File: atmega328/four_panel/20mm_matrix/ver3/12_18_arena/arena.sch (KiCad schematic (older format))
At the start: 50 parts, among them P1 CONN15, P2 CONN15, P3 CONN15, P4 CONN15, P5 CONN15, P6 CONN15, P8 CONN_34X2, P9 CONN_2, Q1 MOSFET_NCHAN, SW1 SWITCH_INV, U1 SPARKFUN_TXB0104, U2 SPARKFUN_TXB0104, U3 SPARKFUN_TXB0104, U4 SPARKFUN_TXB0104, U5 SPARKFUN_TXB0104, U6 SPARKFUN_TXB0104, U8 POLOLU_3V3

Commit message: Finished 12_18 arena schematic.
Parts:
- added C10, C11, C12, C2, C3, C4, C5, C6, C7, C8, C9: C, ~, symbol C
- added C18: 10uf, ~, symbol CP
- added P13, P14, P15, P16, P17, P18, P19, P20, P21, P22, P23, P24: CONN_2, symbol CONN_2
- added R10, R11, R12, R2, R3, R4, R5, R6, R7, R8, R9: R, ~, symbol R
- gave numbers to parts that had none: 20
- renumbered C1 to C13, C2 to C14, C3 to C15, C4 to C16, C5 to C17, P8 to P25, P9 to P26, R3 to R13, R4 to R14, R5 to R15, R6 to R16, R7 to R17, R8 to R18, R1 to R25, R2 to R26, U8 to U13
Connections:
- net 5V: now also C18.1
- net GND: now also C10.2, C11.2, C12.2, C18.2, C2.2, C3.2, C4.2, C5.2, C6.2, C7.2, C8.2, C9.2
- net MISO_10_5V: now also R11.1
- net MISO_11_5V: now also R12.1
- net MISO_1_5V: now also R2.1
- net MISO_2_5V: now also R3.1
- net MISO_3_5V: now also R4.1
- net MISO_4_5V: now also R5.1
- net MISO_5_5V: now also R6.1
- net MISO_6_5V: now also R7.1
- net MISO_7_5V: now also R8.1
- net MISO_8_5V: now also R9.1
- net MISO_9_5V: now also R10.1
- net at C1.1, R1.2: now also P13.2 (PM); no longer U1.11 (B3)
- net at U2.11 (B3): now also P14.1 (P1)
- net at U3.11 (B3): now also P15.1 (P1)
- net at U4.11 (B3): now also P16.1 (P1)
- net at U5.11 (B3): now also P17.1 (P1)
- net at U6.11 (B3): now also P18.1 (P1)
- net at U7.11 (B3): now also P19.1 (P1)
- net at U8.11 (B3): now also P20.1 (P1)
- net at U9.11 (B3): now also P21.1 (P1)
- net at U10.11 (B3): now also P22.1 (P1)
- net at U11.11 (B3): now also P23.1 (P1)
- net at U12.11 (B3): now also P24.1 (P1)
- new net: P13.1 (P1), U1.11 (B3)
- new net: C2.1, P14.2 (PM), R2.2
- new net: C3.1, P15.2 (PM), R3.2
- new net: C4.1, P16.2 (PM), R4.2
- new net: C5.1, P17.2 (PM), R5.2
- new net: C6.1, P18.2 (PM), R6.2
- new net: C7.1, P19.2 (PM), R7.2
- new net: C8.1, P20.2 (PM), R8.2
- new net: C9.1, P21.2 (PM), R9.2
- new net: C10.1, P22.2 (PM), R10.2
- new net: C11.1, P23.2 (PM), R11.2
- new net: C12.1, P24.2 (PM), R12.2
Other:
- moved on the sheet: C1, C13, C14, C15, C16, C17, P1, P10, P11, P12, P2, P25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

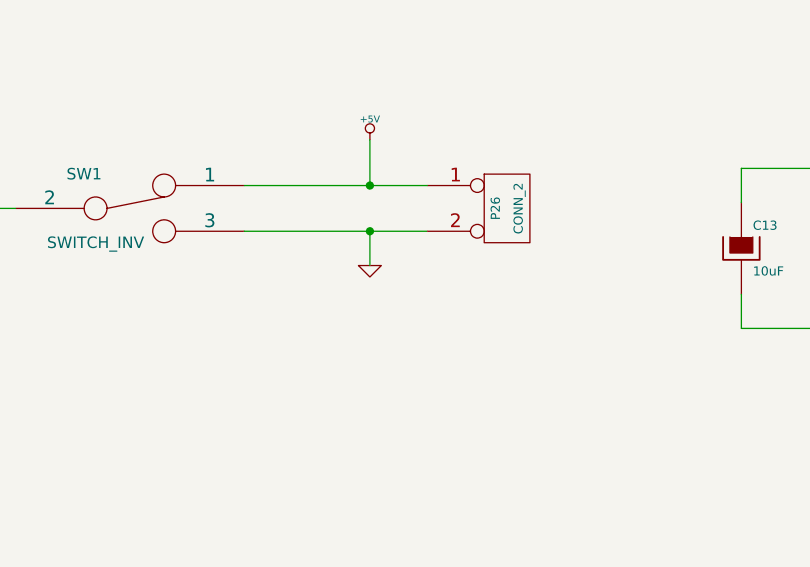
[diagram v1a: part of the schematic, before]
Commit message: Arena modifications.
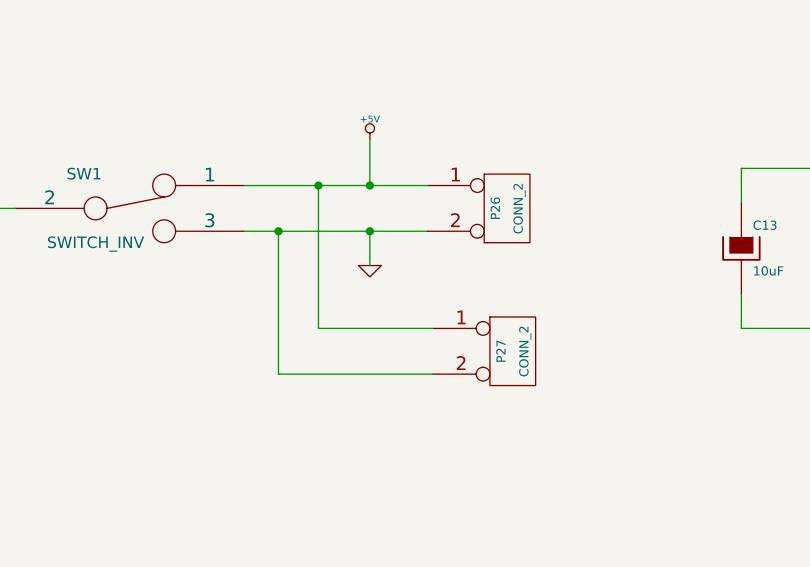
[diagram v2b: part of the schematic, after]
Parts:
- added P27: CONN_2, symbol CONN_2
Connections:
- net +5V: now also P27.1 (P1)
- net GND: now also P27.2 (PM)
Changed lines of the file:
@@
 Sheet 1 1
 Title ""
-Date "8 sep 2015"
+Date "10 sep 2015"
 Rev ""
 Comp ""
@@
 	8550 12250 8550 12500
 Connection ~ 8550 12250
+$Comp
+L CONN_2 P27
+U 1 1 55F1935D
+P 6500 12350
+F 0 "P27" V 6450 12350 40  0000 C CNN
+F 1 "CONN_2" V 6550 12350 40  0000 C CNN
+F 2 "" H 6500 12350 60  0000 C CNN
+F 3 "" H 6500 12350 60  0000 C CNN
+	1    6500 12350
+	1    0    0    -1
+$EndComp
+Wire Wire Line
+	6150 12450 5475 12450
+Wire Wire Line
+	5475 12450 5475 11825
+Connection ~ 5475 11825
+Wire Wire Line
+	6150 12250 5650 12250
+Wire Wire Line
+	5650 12250 5650 11625
+Connection ~ 5650 11625
 $EndSCHEMATC

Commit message: Finished pre-routing layout.
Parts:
- added C19, C20, C21, C22, C23: 10uF, symbol CP
- added P28, P29, P30, P31: CONN_1, symbol CONN_1
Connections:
- net 5V: now also C19.1, C20.1, C21.1, C22.1, C23.1
- net GND: now also C19.2, C20.2, C21.2, C22.2, C23.2, P28.1, P29.1, P30.1, P31.1
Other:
- note added: "Mount holes"
- note removed: "Power"
- moved on the sheet: C13, C14, C15, C16, C17, C18, P26, P27, SW1

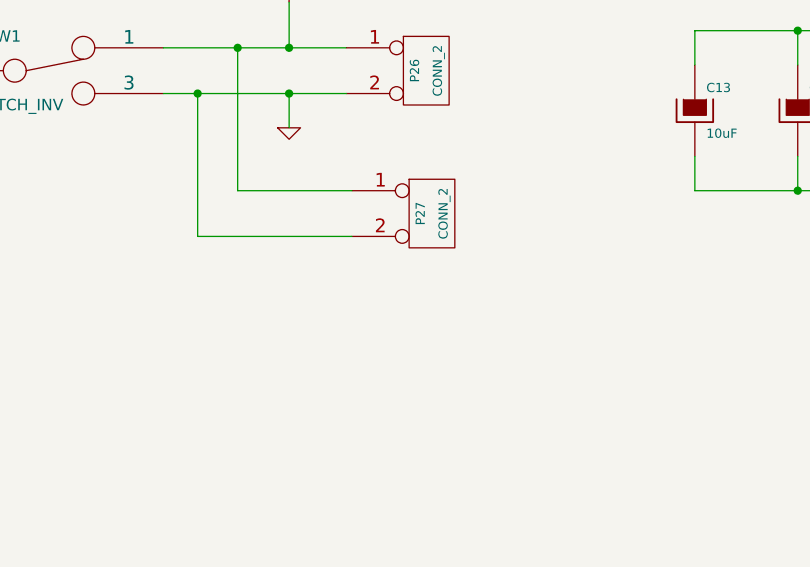
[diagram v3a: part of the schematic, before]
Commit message: Finished design of 12-18 arena. Routed and created gerber files.`
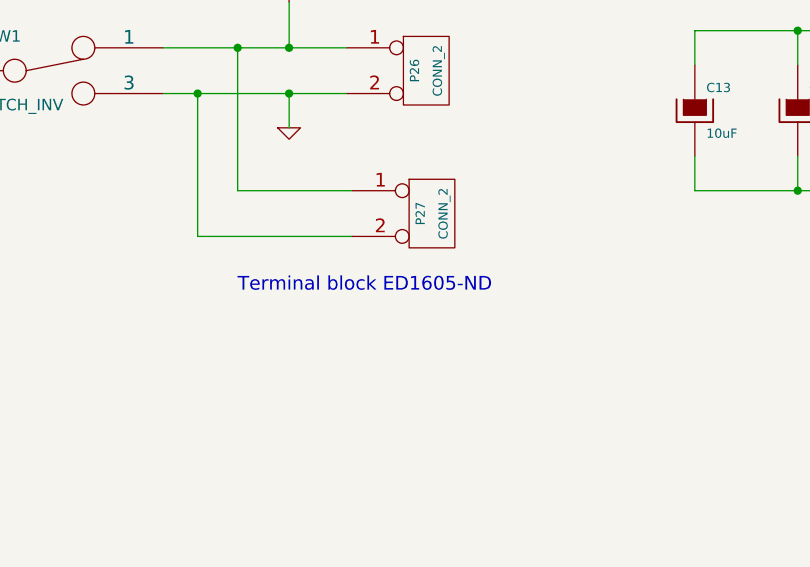
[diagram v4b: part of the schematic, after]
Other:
- note added: "Terminal block ED1605-ND"
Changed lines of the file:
@@
 Text Notes 1600 13800 0    60   ~ 0
 Mount holes
+Text Notes 4350 12650 0    60   ~ 0
+Terminal block ED1605-ND
 $EndSCHEMATC

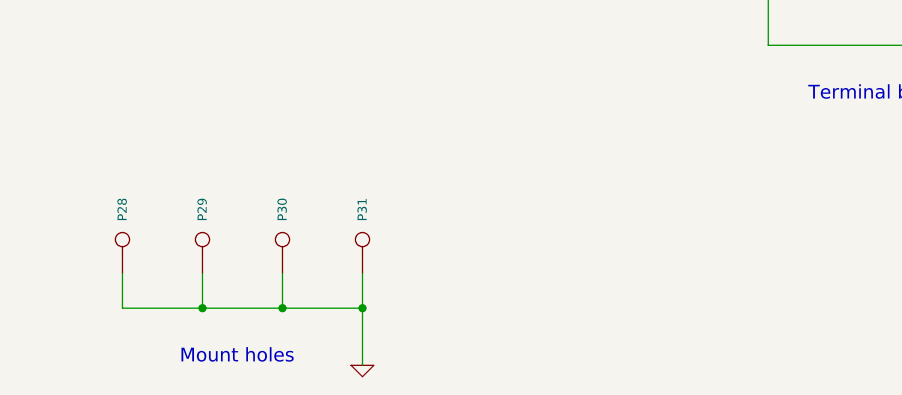
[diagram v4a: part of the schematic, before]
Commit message: Added #4 ground holes.
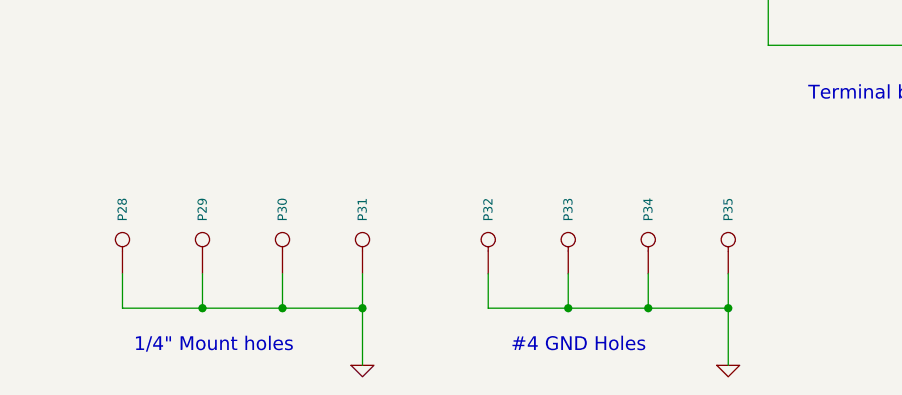
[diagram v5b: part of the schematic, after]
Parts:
- added P32, P33, P34, P35: CONN_1, symbol CONN_1
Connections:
- net GND: now also P32.1, P33.1, P34.1, P35.1
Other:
- note added: "#4 GND Holes"
- note added: "1/4" Mount holes"
- note removed: "Mount holes"

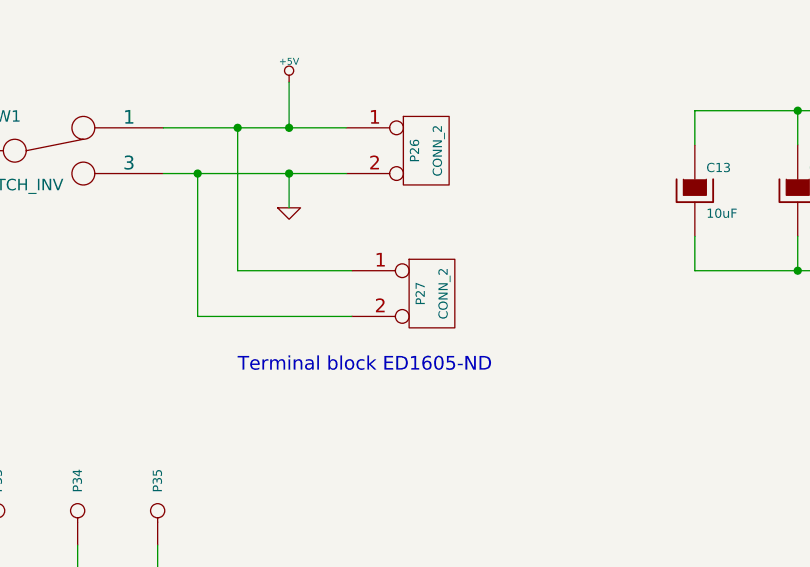
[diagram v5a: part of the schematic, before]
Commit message: Updated BOM for new arena design.
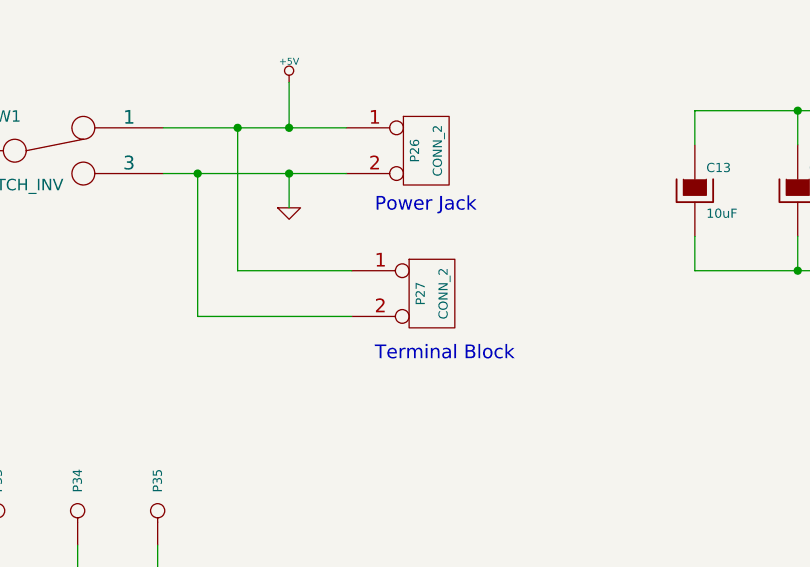
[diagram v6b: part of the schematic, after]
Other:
- note added: "Power Jack"
- note added: "Terminal Block"
- note removed: "Terminal block ED1605-ND"
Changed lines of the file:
@@
 Sheet 1 1
 Title ""
-Date "11 sep 2015"
+Date "5 oct 2015"
 Rev ""
 Comp ""
@@
 Text Notes 1400 13750 0    60   ~ 0
 1/4" Mount holes
-Text Notes 4350 12650 0    60   ~ 0
-Terminal block ED1605-ND
+Text Notes 4950 12600 0    60   ~ 0
+Terminal Block
 $Comp
 L CONN_1 P32
@@
 Text Notes 3050 13750 0    60   ~ 0
 #4 GND Holes
+Text Notes 4950 11950 0    60   ~ 0
+Power Jack
 $EndSCHEMATC

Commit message: Added new version of 12-18 arena.
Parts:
- removed U1, U10, U11, U12, U2, U3, U4, U5, U6, U7, U8, U9: SPARKFUN_TXB0104, ~, symbol SPARKFUN_TXB0104
- removed U13: POLOLU_3V3, ~, symbol POLOLU_3V3
- added C24, C25, C26, C27, C28, C29, C30, C31, C32, C33, C34, C35, C36, C37, C38, C39, C40, C41, C42, C43, C44, C45, C46, C47: 30pF, ~, symbol C
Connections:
- net CS_0_5V is gone; now on net CS_0: P1.7, P10.7, P11.7, P12.7, P2.7, P3.7, P4.7, P5.7, P6.7, P7.7, P8.7, P9.7
- net CS_1_5V is gone; now on net CS_1: P1.8, P10.8, P11.8, P12.8, P2.8, P3.8, P4.8, P5.8, P6.8, P7.8, P8.8, P9.8
- net CS_2_5V is gone; now on net CS_2: P1.9, P10.9, P11.9, P12.9, P2.9, P3.9, P4.9, P5.9, P6.9, P7.9, P8.9, P9.9
- net CS_3_5V is gone; now on net CS_3: P1.10, P10.10, P11.10, P12.10, P2.10, P3.10, P4.10, P5.10, P6.10, P7.10, P8.10, P9.10
- net CS_4_5V is gone; now on net CS_4: P1.11, P10.11, P11.11, P12.11, P2.11, P3.11, P4.11, P5.11, P6.11, P7.11, P8.11, P9.11
- net CS_5_5V is gone; now on net CS_5: P1.12, P10.12, P11.12, P12.12, P2.12, P3.12, P4.12, P5.12, P6.12, P7.12, P8.12, P9.12
- net CS_6_5V is gone; now on net CS_6: P1.13, P10.13, P11.13, P12.13, P2.13, P3.13, P4.13, P5.13, P6.13, P7.13, P8.13, P9.13
- net CS_7_5V is gone; now on net CS_7: P1.14, P10.14, P11.14, P12.14, P2.14, P3.14, P4.14, P5.14, P6.14, P7.14, P8.14, P9.14
- net EXT_INT_5V is gone; now on net EXT_INT: P1.15, P10.15, P11.15, P12.15, P2.15, P3.15, P4.15, P5.15, P6.15, P7.15, P8.15, P9.15
- net MOSI_0_5V is gone; now on net MOSI_0: P1.5
- net MOSI_10_5V is gone; now on net MOSI_10: P11.5
- net MOSI_11_5V is gone; now on net MOSI_11: P12.5
- net MOSI_1_5V is gone; now on net MOSI_1: P2.5
- net MOSI_2_5V is gone; now on net MOSI_2: P3.5
- net MOSI_3_5V is gone; now on net MOSI_3: P4.5
- net MOSI_4_5V is gone; now on net MOSI_4: P5.5
- net MOSI_5_5V is gone; now on net MOSI_5: P6.5
- net MOSI_6_5V is gone; now on net MOSI_6: P7.5
- net MOSI_7_5V is gone; now on net MOSI_7: P8.5
- net MOSI_8_5V is gone; now on net MOSI_8: P9.5
- net MOSI_9_5V is gone; now on net MOSI_9: P10.5
- net SCK_0_5V is gone; now on net SCK_0: P1.4
- net SCK_1_5V is gone; now on net SCK_1: P2.4
- net SCK_2_5V is gone; now on net SCK_2: P3.4
- net SCK_3_5V is gone; now on net SCK_3: P4.4
- net SCK_4_3V3 is gone; now on net SCK_4: P25.47 (P47)
- net SCK_4_5V is gone; now on net SCK_4: P5.4
- net SCK_5_3V3 is gone; now on net SCK_5: P25.48 (P48)
- net SCK_5_5V is gone; now on net SCK_5: P6.4
- net SCK_6_5V is gone; now on net SCK_0: P7.4
- net SCK_7_5V is gone; now on net SCK_1: P8.4
- net SCK_8_5V is gone; now on net SCK_2: P9.4
- net SCK_9_5V is gone; now on net SCK_3: P10.4
- net GND: now also C24.2, C25.2, C26.2, C27.2, C28.2, C29.2, C30.2, C31.2, C32.2, C33.2, C34.2, C35.2, C36.2, C37.2, C38.2, C39.2, C40.2, C41.2, C42.2, C43.2, C44.2, C45.2, C46.2, C47.2
- net at R13.1: now also P13.1 (P1)
- net at R14.1: now also P14.1 (P1)
- net at R15.1: now also P15.1 (P1)
- net at R16.1: now also P16.1 (P1)
- net at R17.1: now also P17.1 (P1)
- net at R18.1: now also P18.1 (P1)
- net at R19.1: now also P19.1 (P1)
- net at R20.1: now also P20.1 (P1)
- net at R21.1: now also P21.1 (P1)
- net at R22.1: now also P22.1 (P1)
- net at R23.1: now also P23.1 (P1)
- net at R24.1: now also P24.1 (P1)
- net CS_0_3V3 renamed CS_0
- net CS_0: now also C24.1, C25.1, C26.1
- net CS_1_3V3 renamed CS_1
- net CS_1: now also C27.1, C28.1, C29.1
- net CS_2_3V3 renamed CS_2
- net CS_2: now also C30.1, C31.1, C32.1
- net CS_3_3V3 renamed CS_3
- net CS_3: now also C33.1, C34.1, C35.1
- net CS_4_3V3 renamed CS_4
- net CS_4: now also C36.1, C37.1, C38.1
- net CS_5_3V3 renamed CS_5
- net CS_5: now also C39.1, C40.1, C41.1
- net CS_6_3V3 renamed CS_6
- net CS_6: now also C42.1, C43.1, C44.1
- net CS_7_3V3 renamed CS_7
- net CS_7: now also C45.1, C46.1, C47.1
- net EXT_INT_3V3 renamed EXT_INT
- net MISO_0_3V3 renamed MISO_0
- net MISO_0_5V renamed _MISO_0
- net MISO_10_3V3 renamed MISO_10
- net MISO_10_5V renamed _MISO_10
- net MISO_11_3V3 renamed MISO_11
- net MISO_11_5V renamed _MISO_11
- net MISO_1_3V3 renamed MISO_1
- net MISO_1_5V renamed _MISO_1
- net MISO_2_3V3 renamed MISO_2
- net MISO_2_5V renamed _MISO_2
- net MISO_3_3V3 renamed MISO_3
- net MISO_3_5V renamed _MISO_3
- net MISO_4_3V3 renamed MISO_4
- net MISO_4_5V renamed _MISO_4
- net MISO_5_3V3 renamed MISO_5
- net MISO_5_5V renamed _MISO_5
- net MISO_6_3V3 renamed MISO_6
- net MISO_6_5V renamed _MISO_6
- net MISO_7_3V3 renamed MISO_7
- net MISO_7_5V renamed _MISO_7
- net MISO_8_3V3 renamed MISO_8
- net MISO_8_5V renamed _MISO_8
- net MISO_9_3V3 renamed MISO_9
- net MISO_9_5V renamed _MISO_9
- net MOSI_0_3V3 renamed MOSI_0
- net MOSI_10_3V3 renamed MOSI_10
- net MOSI_11_3V3 renamed MOSI_11
- net MOSI_1_3V3 renamed MOSI_1
- net MOSI_2_3V3 renamed MOSI_2
- net MOSI_3_3V3 renamed MOSI_3
- net MOSI_4_3V3 renamed MOSI_4
- net MOSI_5_3V3 renamed MOSI_5
- net MOSI_6_3V3 renamed MOSI_6
- net MOSI_7_3V3 renamed MOSI_7
- net MOSI_8_3V3 renamed MOSI_8
- net MOSI_9_3V3 renamed MOSI_9
- net SCK_0_3V3 renamed SCK_0
- net SCK_10_5V renamed SCK_4
- net SCK_11_5V renamed SCK_5
- net SCK_1_3V3 renamed SCK_1
- net SCK_2_3V3 renamed SCK_2
- net SCK_3_3V3 renamed SCK_3
- no-connect marks 57 -> 26
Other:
- moved on the sheet: C13, C14, C15, C16, C17, C18, C19, C20, C21, C22, C23, P25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
